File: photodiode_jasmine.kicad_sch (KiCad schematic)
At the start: 1 part

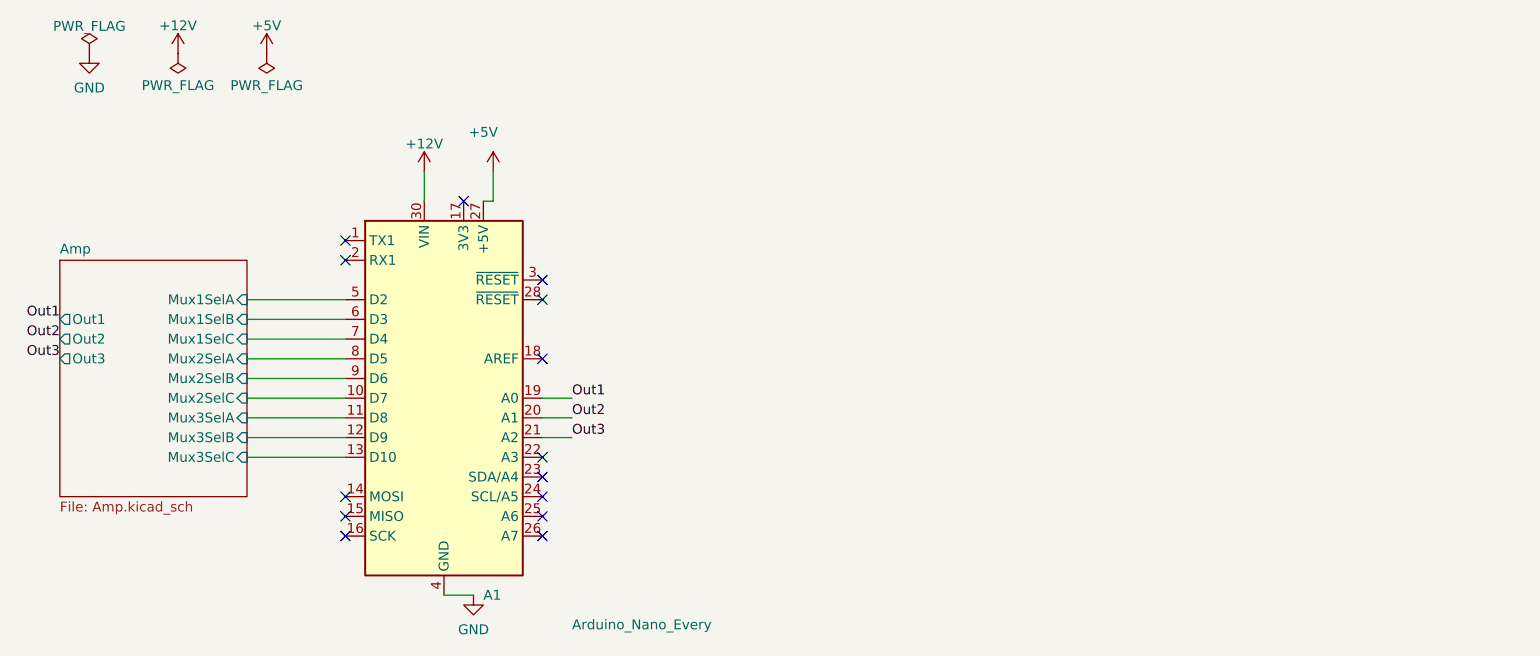
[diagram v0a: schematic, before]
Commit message: Added photodiode connector, haven't routed
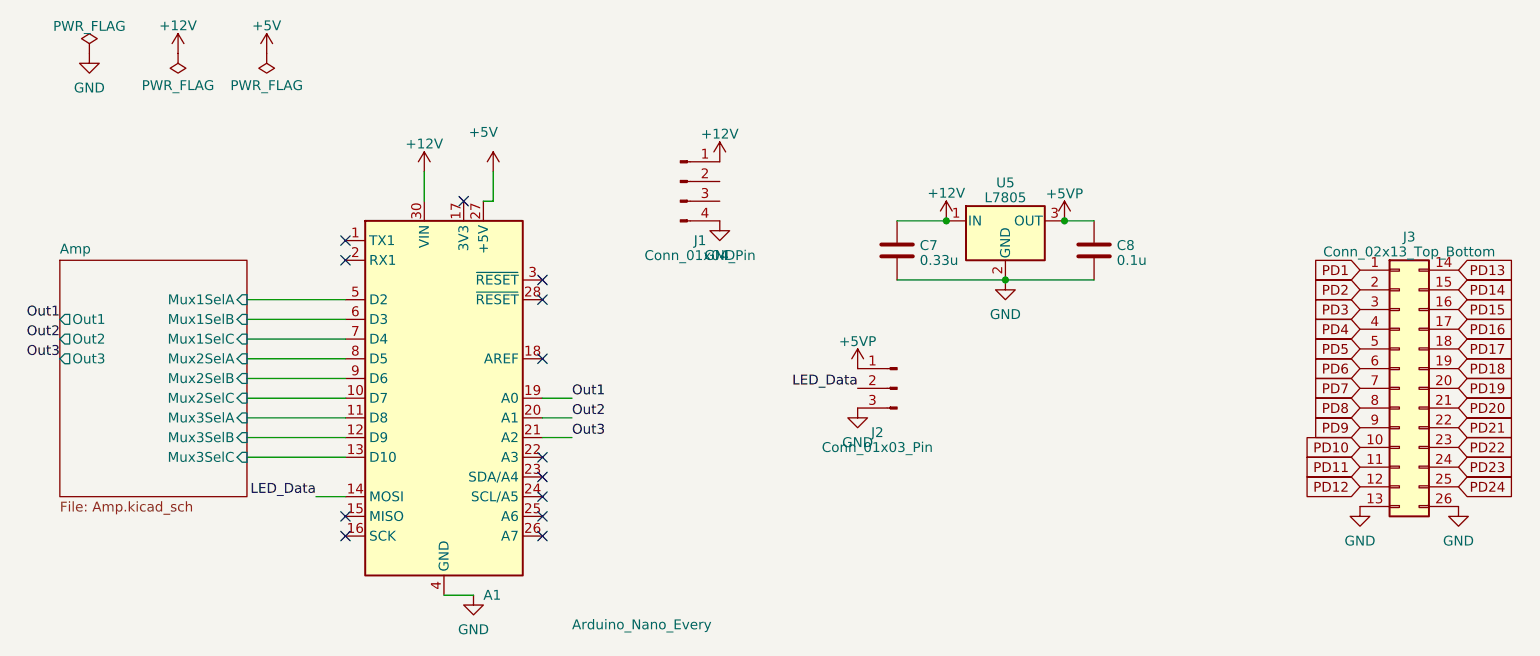
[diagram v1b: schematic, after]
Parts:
- added C7: 0.33u, symbol Device:C
- added C8: 0.1u, symbol Device:C
- added J1: Conn_01x04_Pin, Connector_PinHeader_2.54mm:PinHeader_1x04_P2.54mm_Vertical, symbol Connector:Conn_01x04_Pin
- added J2: Conn_01x03_Pin, Connector_PinHeader_2.54mm:PinHeader_1x03_P2.54mm_Vertical, symbol Connector:Conn_01x03_Pin
- added J3: Conn_02x13_Top_Bottom, Connector_PinHeader_2.54mm:PinHeader_2x13_P2.54mm_Vertical, symbol Connector_Generic:Conn_02x13_Top_Bottom
- added U5: L7805, Package_TO_SOT_THT:TO-220-3_Horizontal_TabDown, symbol Regulator_Linear:L7805
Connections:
- net +12V: now also C7.1, J1.1 (Pin_1), U5.1 (IN)
- net GND: now also C7.2, C8.2, J1.4 (Pin_4), J2.3 (Pin_3), J3.13 (Pin_13), J3.26 (Pin_26), U5.2 (GND)
- net LED_Data: now reaches A1.14 (MOSI)
- net LED_Data: now also J2.2 (Pin_2)
- new net +5VP: C8.1, J2.1 (Pin_1), U5.3 (OUT)
- new net PD1: J3.1 (Pin_1)
- new net PD10: J3.10 (Pin_10)
- new net PD11: J3.11 (Pin_11)
- new net PD12: J3.12 (Pin_12)
- new net PD13: J3.14 (Pin_14)
- new net PD14: J3.15 (Pin_15)
- new net PD15: J3.16 (Pin_16)
- new net PD16: J3.17 (Pin_17)
- new net PD17: J3.18 (Pin_18)
- new net PD18: J3.19 (Pin_19)
- new net PD19: J3.20 (Pin_20)
- new net PD2: J3.2 (Pin_2)
- new net PD20: J3.21 (Pin_21)
- new net PD21: J3.22 (Pin_22)
- new net PD22: J3.23 (Pin_23)
- new net PD23: J3.24 (Pin_24)
- new net PD24: J3.25 (Pin_25)
- new net PD3: J3.3 (Pin_3)
- new net PD4: J3.4 (Pin_4)
- new net PD5: J3.5 (Pin_5)
- new net PD6: J3.6 (Pin_6)
- new net PD7: J3.7 (Pin_7)
- new net PD8: J3.8 (Pin_8)
- new net PD9: J3.9 (Pin_9)
- no-connect marks 14 -> 13

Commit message: Not sure what's changed
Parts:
- C7, C8: footprint (none) -> Capacitor_THT:C_Disc_D5.1mm_W3.2mm_P5.00mm
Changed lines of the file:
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@@
       (effects (font (size 1.27 1.27)) (justify left))
     )
-    (property "Footprint" "" (at 201.6252 48.26 0)
+    (property "Footprint" "Capacitor_THT:C_Disc_D5.1mm_W3.2mm_P5.00mm" (at 201.6252 48.26 0)
       (effects (font (size 1.27 1.27)) hide)
     )
@@
       (effects (font (size 1.27 1.27)) (justify left))
     )
-    (property "Footprint" "" (at 176.2252 48.26 0)
-      (effects (font (size 1.27 1.27)) hide)
-    )
+    (property "Footprint" "Capacitor_THT:C_Disc_D5.1mm_W3.2mm_P5.00mm" (at 176.2252 48.26 0)
+      (effects (font (size 1.27 1.27)) hide)
+    )
